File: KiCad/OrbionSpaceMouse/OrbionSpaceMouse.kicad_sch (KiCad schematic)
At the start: 5 parts

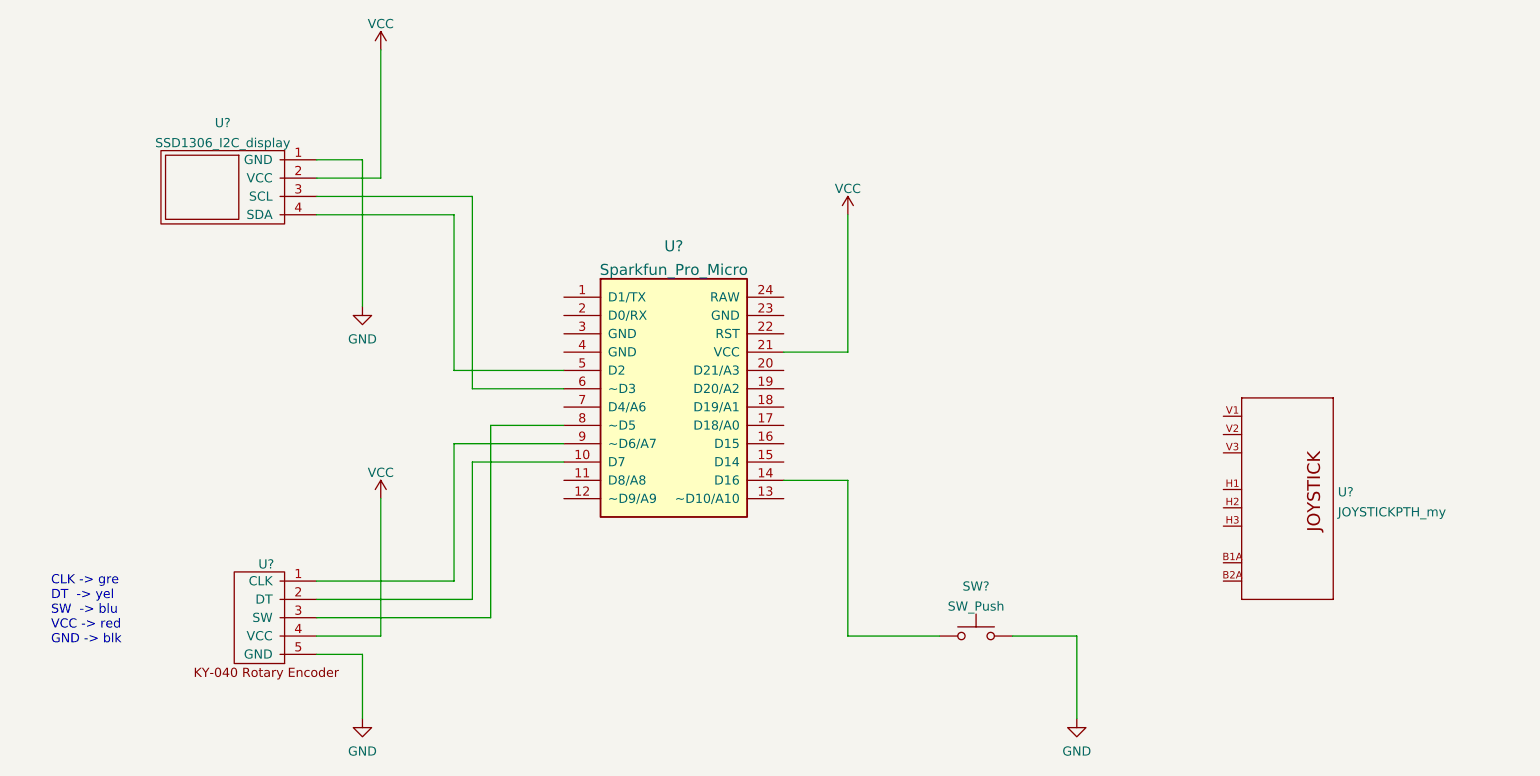
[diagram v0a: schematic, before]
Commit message: added joystick
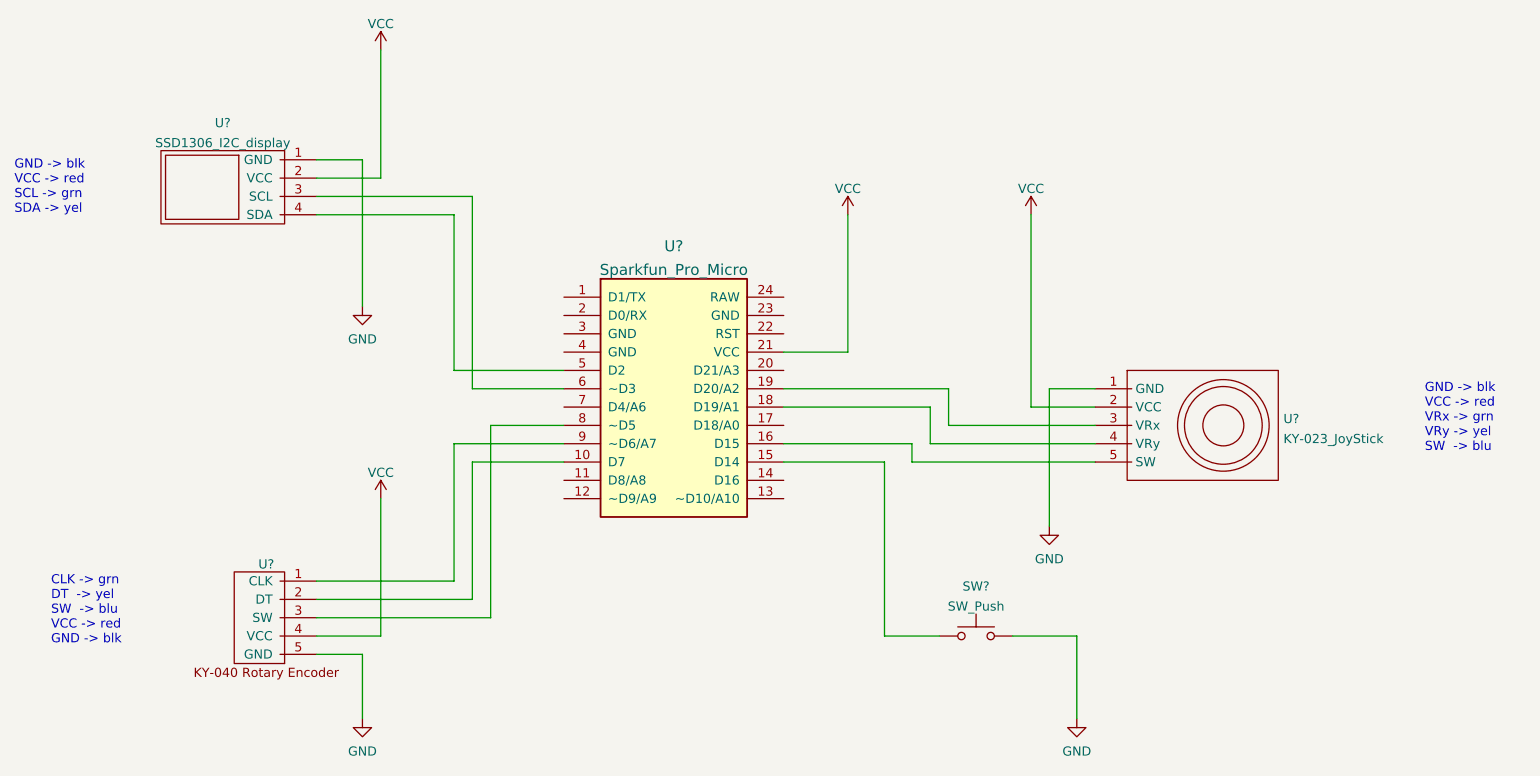
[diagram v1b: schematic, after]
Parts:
- removed U?: JOYSTICKPTH_my, JOYSTICK, symbol SparkFun_Electromechanical:JOYSTICKPTH_my
- added U?: KY-023_JoyStick, symbol My_Parts:KY-023_JoyStick
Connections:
- net GND: now also U?.1 (GND)
- net VCC: now also U?.2 (VCC)
- net at SW?.1: now also U?.15 (D14); no longer U?.14 (D16)
- net at U?.16 (D15): now also U?.5 (SW)
- net at U?.18 (D19/A1): now also U?.4 (VRy)
- net at U?.19 (D20/A2): now also U?.3 (VRx)
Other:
- note added: "CLK -> grn DT -> yel SW -> blu VCC -> red GND -> blk"
- note added: "GND -> blk VCC -> red SCL -> grn SDA -> yel"
- note added: "GND -> blk VCC -> red VRx -> grn VRy -> yel SW -> blu"
- note removed: "CLK -> gre DT -> yel SW -> blu VCC -> red GND -> blk"
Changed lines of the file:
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@@
+    (stroke (width 0) (type default) (color 0 0 0 0))
+  )
+  (wire (pts (xy 200.66 107.95) (xy 175.26 107.95))
+    (stroke (width 0) (type default) (color 0 0 0 0))
+  )
+  (wire (pts (xy 179.07 132.08) (xy 171.45 132.08))
     (stroke (width 0) (type default) (color 0 0 0 0))
   )
@@
     (stroke (width 0) (type default) (color 0 0 0 0))
   )
+  (wire (pts (xy 200.66 105.41) (xy 177.8 105.41))
+    (stroke (width 0) (type default) (color 0 0 0 0))
+  )
   (wire (pts (xy 99.06 134.62) (xy 99.06 143.51))
     (stroke (width 0) (type default) (color 0 0 0 0))
   )
+  (wire (pts (xy 175.26 107.95) (xy 175.26 105.41))
+    (stroke (width 0) (type default) (color 0 0 0 0))
+  )
+  (wire (pts (xy 200.66 100.33) (xy 191.77 100.33))
+    (stroke (width 0) (type default) (color 0 0 0 0))
+  )
+  (wire (pts (xy 191.77 100.33) (xy 191.77 73.66))
+    (stroke (width 0) (type default) (color 0 0 0 0))
+  )
   (wire (pts (xy 116.84 129.54) (xy 116.84 102.87))
     (stroke (width 0) (type default) (color 0 0 0 0))
@@
     (stroke (width 0) (type default) (color 0 0 0 0))
   )
+  (wire (pts (xy 180.34 97.79) (xy 180.34 102.87))
+    (stroke (width 0) (type default) (color 0 0 0 0))
+  )
+  (wire (pts (xy 194.31 97.79) (xy 194.31 116.84))
+    (stroke (width 0) (type default) (color 0 0 0 0))
+  )
   (wire (pts (xy 116.84 102.87) (xy 127 102.87))
     (stroke (width 0) (type default) (color 0 0 0 0))
@@
     (stroke (width 0) (type default) (color 0 0 0 0))
   )
-  (wire (pts (xy 166.37 132.08) (xy 166.37 110.49))
-    (stroke (width 0) (type default) (color 0 0 0 0))
-  )
   (wire (pts (xy 111.76 105.41) (xy 127 105.41))
     (stroke (width 0) (type default) (color 0 0 0 0))
@@
     (stroke (width 0) (type default) (color 0 0 0 0))
   )
+  (wire (pts (xy 177.8 105.41) (xy 177.8 100.33))
+    (stroke (width 0) (type default) (color 0 0 0 0))
+  )
   (wire (pts (xy 92.71 66.04) (xy 99.06 66.04))
     (stroke (width 0) (type default) (color 0 0 0 0))
   )
+  (wire (pts (xy 157.48 97.79) (xy 180.34 97.79))
+    (stroke (width 0) (type default) (color 0 0 0 0))
+  )
+  (wire (pts (xy 177.8 100.33) (xy 157.48 100.33))
+    (stroke (width 0) (type default) (color 0 0 0 0))
+  )
   (wire (pts (xy 114.3 107.95) (xy 127 107.95))
     (stroke (width 0) (type default) (color 0 0 0 0))
@@
     (stroke (width 0) (type default) (color 0 0 0 0))
   )
+  (wire (pts (xy 180.34 102.87) (xy 200.66 102.87))
+    (stroke (width 0) (type default) (color 0 0 0 0))
+  )
+  (wire (pts (xy 200.66 97.79) (xy 194.31 97.79))
+    (stroke (width 0) (type default) (color 0 0 0 0))
+  )
   (wire (pts (xy 92.71 124.46) (xy 111.76 124.46))
     (stroke (width 0) (type default) (color 0 0 0 0))
@@
     (stroke (width 0) (type default) (color 0 0 0 0))
   )
-  (wire (pts (xy 166.37 110.49) (xy 157.48 110.49))
+  (wire (pts (xy 157.48 105.41) (xy 175.26 105.41))
     (stroke (width 0) (type default) (color 0 0 0 0))
   )
@@
     (stroke (width 0) (type default) (color 0 0 0 0))
   )
-  (wire (pts (xy 179.07 132.08) (xy 166.37 132.08))
-    (stroke (width 0) (type default) (color 0 0 0 0))
-  )
-  (text "CLK -> gre\nDT  -> yel\nSW  -> blu\nVCC -> red\nGND -> blk"
+  (wire (pts (xy 171.45 107.95) (xy 157.48 107.95))
+    (stroke (width 0) (type default) (color 0 0 0 0))
+  )
+  (wire (pts (xy 171.45 132.08) (xy 171.45 107.95))
+    (stroke (width 0) (type default) (color 0 0 0 0))
+  )
+  (text "GND -> blk\nVCC -> red\nSCL -> grn\nSDA -> yel" (at 50.8 73.66 0)
+    (effects (font (size 1.27 1.27)) (justify left bottom))
+  )
+  (text "GND -> blk\nVCC -> red\nVRx -> grn\nVRy -> yel\nSW  -> blu"
+    (at 246.38 106.68 0)
+    (effects (font (size 1.27 1.27)) (justify left bottom))
+  )
+  (text "CLK -> grn\nDT  -> yel\nSW  -> blu\nVCC -> red\nGND -> blk"
     (at 55.88 133.35 0)
     (effects (font (size 1.27 1.27)) (justify left bottom))
@@
     )
     (pin "1")
+  )
+  (symbol (lib_id "My_Parts:KY-023_JoyStick") (at 200.66 97.79 0) (unit 1)
+    (in_bom yes) (on_board yes) (fields_autoplaced)
+    (property "Reference" "U?" (id 0) (at 226.7712 101.9615 0)
+      (effects (font (size 1.27 1.27)) (justify left))
+    )
+    (property "Value" "KY-023_JoyStick" (id 1) (at 226.7712 104.7366 0)
+      (effects (font (size 1.27 1.27)) (justify left))
+    )
+    (property "Footprint" "" (id 2) (at 207.01 93.98 0)
+      (effects (font (size 1.27 1.27)) hide)
+    )
+    (property "Datasheet" "" (id 3) (at 207.01 93.98 0)
+      (effects (font (size 1.27 1.27)) hide)
+    )
+    (pin "1")
+    (pin "2")
+    (pin "3")
+    (pin "4")
+    (pin "5")
   )
   (symbol (lib_id "Switch:SW_Push") (at 184.15 132.08 0) (unit 1)
@@
     (pin "1")
     (pin "2")
+  )
+  (symbol (lib_id "power:GND") (at 194.31 116.84 0) (unit 1)
+    (in_bom yes) (on_board yes) (fields_autoplaced)
+    (property "Reference" "#PWR?" (id 0) (at 194.31 123.19 0)
+      (effects (font (size 1.27 1.27)) hide)
+    )
+    (property "Value" "GND" (id 1) (at 194.31 121.4025 0))
+    (property "Footprint" "" (id 2) (at 194.31 116.84 0)
+      (effects (font (size 1.27 1.27)) hide)
+    )
+    (property "Datasheet" "" (id 3) (at 194.31 116.84 0)
+      (effects (font (size 1.27 1.27)) hide)
+    )
+    (pin "1")
+  )
+  (symbol (lib_id "power:VCC") (at 191.77 73.66 0) (unit 1)
+    (in_bom yes) (on_board yes) (fields_autoplaced)
+    (property "Reference" "#PWR?" (id 0) (at 191.77 77.47 0)
+      (effects (font (size 1.27 1.27)) hide)
+    )
+    (property "Value" "VCC" (id 1) (at 191.77 70.0555 0))
+    (property "Footprint" "" (id 2) (at 191.77 73.66 0)
+      (effects (font (size 1.27 1.27)) hide)
+    )
+    (property "Datasheet" "" (id 3) (at 191.77 73.66 0)
+      (effects (font (size 1.27 1.27)) hide)
+    )
+    (pin "1")
   )
   (symbol (lib_id "power:VCC") (at 101.6 50.8 0) (unit 1)
@@
     (pin "5")
   )
-  (symbol (lib_id "SparkFun_Electromechanical:JOYSTICKPTH_my") (at 228.6 111.76 0) (unit 1)
-    (in_bom yes) (on_board yes) (fields_autoplaced)
-    (property "Reference" "U?" (id 0) (at 234.315 112.1215 0)
-      (effects (font (size 1.27 1.27)) (justify left))
-    )
-    (property "Value" "JOYSTICKPTH_my" (id 1) (at 234.315 114.8966 0)
-      (effects (font (size 1.27 1.27)) (justify left))
-    )
-    (property "Footprint" "JOYSTICK" (id 2) (at 229.362 107.95 0)
-      (effects (font (size 0.508 0.508)) hide)
-    )
-    (property "Datasheet" "" (id 3) (at 228.6 111.76 0)
-      (effects (font (size 1.27 1.27)) hide)
-    )
-    (pin "B1B")
-    (pin "B2B")
-    (pin "B1A")
-    (pin "B2A")
-    (pin "H1")
-    (pin "H2")
-    (pin "H3")
-    (pin "V1")
-    (pin "V2")
-    (pin "V3")
-  )
   (symbol (lib_id "power:VCC") (at 166.37 73.66 0) (unit 1)
     (in_bom yes) (on_board yes) (fields_autoplaced)
@@
       (reference "#PWR?") (unit 1) (value "GND") (footprint "")
     )
+    (path "/581b02e0-e61c-4e78-b948-a79ce3a4d8f3"
+      (reference "#PWR?") (unit 1) (value "GND") (footprint "")
+    )
+    (path "/5e54d0df-56d4-4018-9d15-b38fdba651d4"
+      (reference "#PWR?") (unit 1) (value "VCC") (footprint "")
+    )
     (path "/70dff86c-3471-46b6-bc2b-9ba0f3f8fe5d"
       (reference "#PWR?") (unit 1) (value "VCC") (footprint "")
@@
       (reference "SW?") (unit 1) (value "SW_Push") (footprint "")
     )
+    (path "/42df0aa5-95ee-4285-88f5-dbb30410b3cd"
+      (reference "U?") (unit 1) (value "KY-023_JoyStick") (footprint "")
+    )
     (path "/87371631-aa02-498a-998a-09bdb74784c1"
       (reference "U?") (unit 1) (value "Sparkfun_Pro_Micro") (footprint "Arduino:Sparkfun_Pro_Micro")
@@
       (reference "U?") (unit 1) (value "KY-040_Rotary_Encoder") (footprint "")
     )
-    (path "/d40ed1bf-6a69-492a-acf3-f71f1c7a81f2"
-      (reference "U?") (unit 1) (value "JOYSTICKPTH_my") (footprint "JOYSTICK")
-    )
     (path "/f3ae8f97-c968-4274-a953-333d18cbf40c"
